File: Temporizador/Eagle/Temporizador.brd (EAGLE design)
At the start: 118.6 x 59.2 mm, 32 parts, among them IC1 7805TV, J1 DCJ0202, Q1 BD139

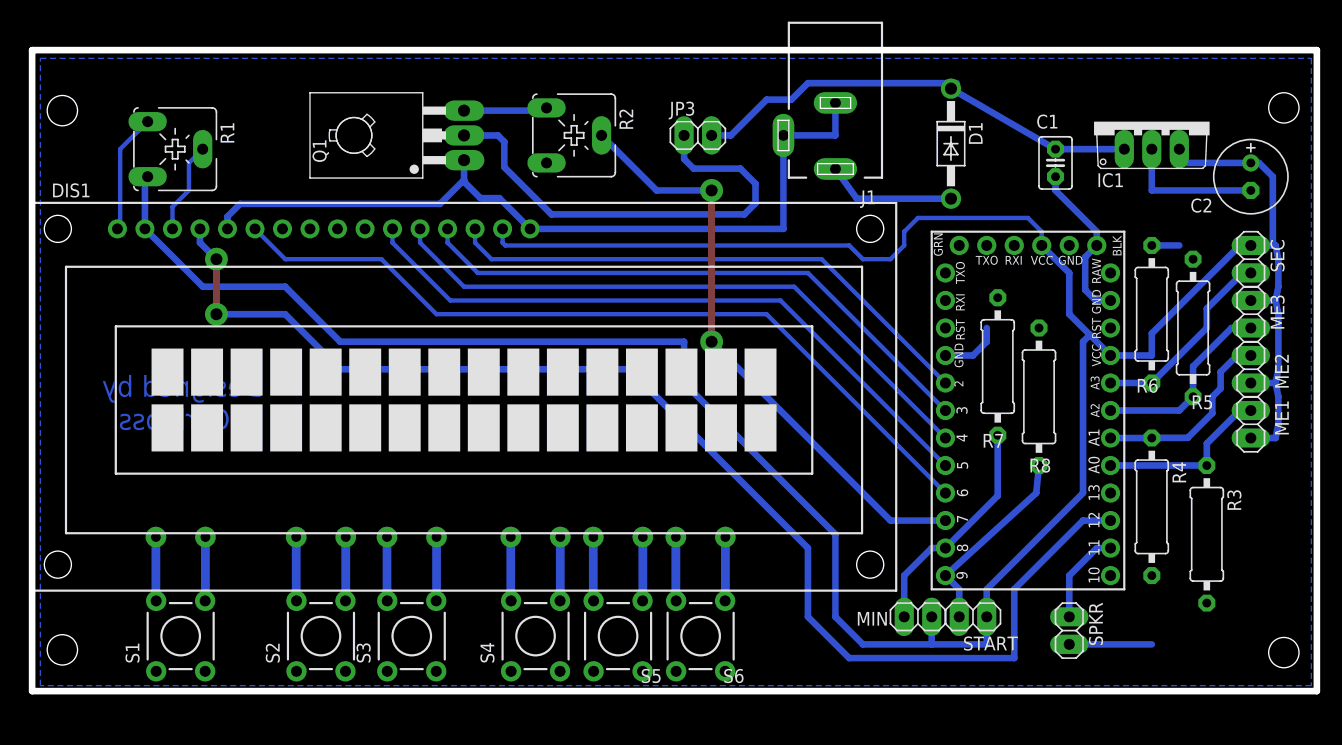
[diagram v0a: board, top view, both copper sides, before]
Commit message: Board v1.2
Added more useful pins, comments and larger pads for better soldering
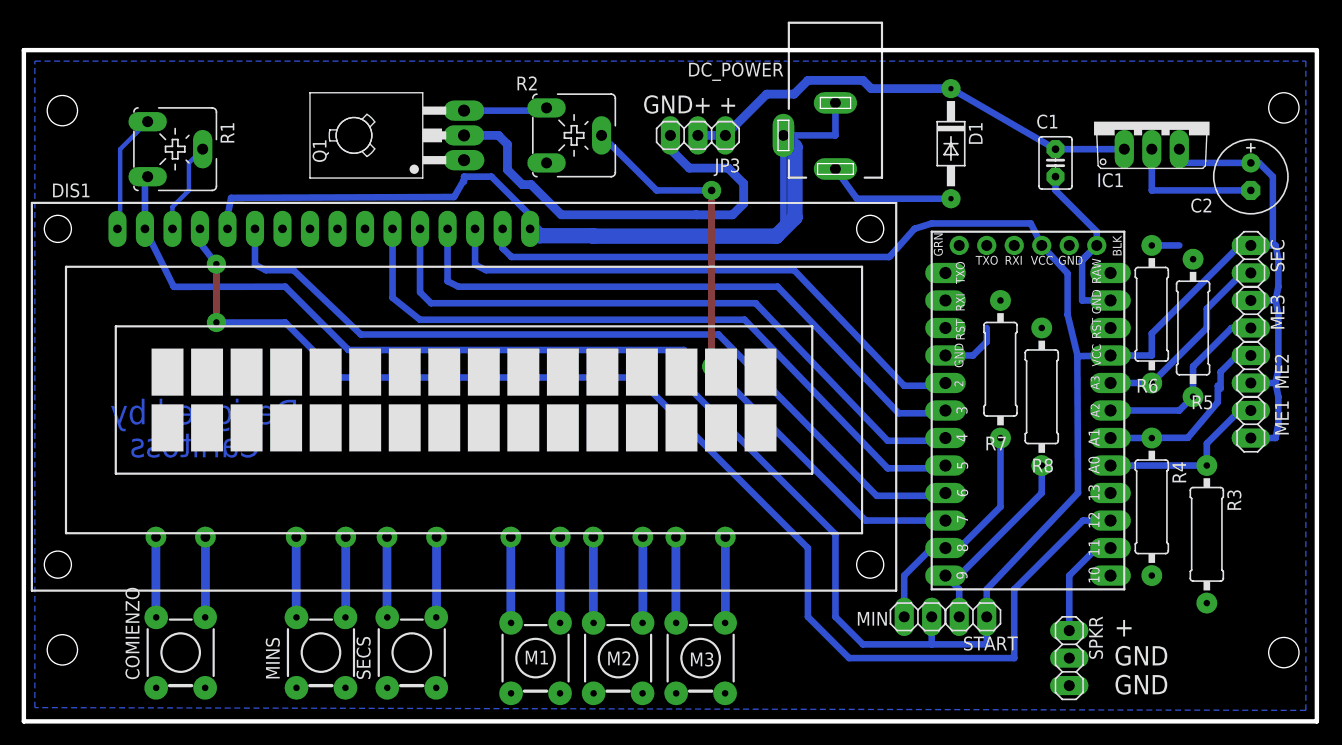
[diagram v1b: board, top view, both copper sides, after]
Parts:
- removed S1, S2, S3, S4, S5, S6: (no value), SparkFun-Electromechanical:TACTILE-PTH
- added COMIENZO, M1, M2, M3, MINS, SECS: (no value), SparkFun-Electromechanical:TACTILE-PTH
- JP3, SPKR: device pinhead:1X02 -> pinhead:1X03
- JP6, JP7: device SparkFun:1X12 -> SparkFun-Connectors:1X12_LONGPADS
- R2: value (none) -> 100k
- moved SPKR 2.54 mm to (12.7, -8.89)
- moved R7 0.36 mm to (6.35, 17.8)
- moved R8 0.25 mm to (10.2, 15.2)
- renumbered J1 to DC_POWER
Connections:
- net +14V: now also JP3.3
- net GND: now also SPKR.3
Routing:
- net GND: track 129.1 -> 135.4 mm
- net D5: track 60.9 -> 64.1 mm
- net D4: track 57.3 -> 60.3 mm
- net D3: track 53.7 -> 56.0 mm
- net D6: track 73.9 -> 75.9 mm
- net N$19: track 6.10 -> 8.13 mm
- net N$18: track 6.10 -> 8.13 mm
- net N$17: track 6.10 -> 8.13 mm
- net N$16: track 6.10 -> 8.13 mm
- net N$15: track 6.10 -> 8.13 mm
- net N$14: track 6.10 -> 8.13 mm
- net VCC: track 271.4 -> 269.7 mm
- net N$9: track 6.10 -> 7.62 mm
- net N$8: track 6.10 -> 7.62 mm
- net N$13: track 6.10 -> 7.62 mm
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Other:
- board size 118.6 x 59.2 mm -> 119.4 x 62 mm
- board text added: "+ GND GND"
- board text added: "GND+ +"
